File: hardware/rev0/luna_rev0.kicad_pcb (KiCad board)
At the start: 4 copper layers, 48.9 x 50 mm, 132 parts, among them IC1 ECP5-BGA256, J1 USB_B_Micro, J2 USB_B_Micro, J3 USB_A, J4 USB_B_Micro, J5 Conn_ARM_JTAG_SWD_10, J6 Conn_ARM_JTAG_SWD_10, J7 Conn_02x02_Counter_Clockwise, J8 Conn_Coaxial, J9 Conn_Coaxial, SW1 BTN_RECOVERY, SW2 BTN_DFU, SW3 BTN_RESET, U1 AP22814-SOT, U10 S27KS0641, U11 USB3343, U12 AP22814-SOT, U2 MIC5504-1.8YM5, U3 MIC5219-3.3YM5, U4 TCR2EE11, U5 MIC5504-2.5YM5, U6 ATSAMD21G18A-AUT, U7 W25Q32JVSS, U8 USB3343, U9 USB3343, Y1 DSC60xx

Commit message: hardware: rev0.2 (FFY00 + perigoso)
Signed-off-by: Filipe Laíns <lains@archlinux.org>
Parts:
- added G***: LOGO, ffy00-modules:brasao-smaller, B.Cu at (112.4, 90.2)
- J5, J6: footprint luna:SWD_CONNECTOR_LARGE_BOX -> Connector_PinHeader_2.00mm:PinHeader_2x05_P2.00mm_Vertical
- moved REF** 30.8 mm to (134.6, 73.7)
- moved J5 5.23 mm to (137.9, 100.8), turned to -90 degrees
- moved J6 2.98 mm to (129.9, 108.4), turned to 90 degrees
- moved G*** 1.74 mm to (97.8, 108.1)
- moved R25 1.65 mm to (140.1, 107.3)
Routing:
- net /FULL_RESET: track 34.6 -> 40.9 mm
- net /FPGA Configuration and Dev Features/FPGA_TMS: track 25.4 -> 28.1 mm
- net /FPGA Configuration and Dev Features/FPGA_TCK: track 23.7 -> 25.7 mm
- net /FPGA Configuration and Dev Features/FPGA_TDO: track 25.4 -> 26.7 mm
- net /FPGA Configuration and Dev Features/UC_SWDCLK: track 13.6 -> 14.8 mm
- net GND: track 180.0 -> 180.8 mm
- net /FPGA Configuration and Dev Features/FPGA_TDI: track 20.5 -> 21.1 mm
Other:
- net class Default removed
- board text added: "Filipe Laíns @FFY00 Rafael Silva @perigoso"
- board text added: "Manufactured by"
- board text removed: "3 G 0 2 G 1"
- board text removed: "A-Side"

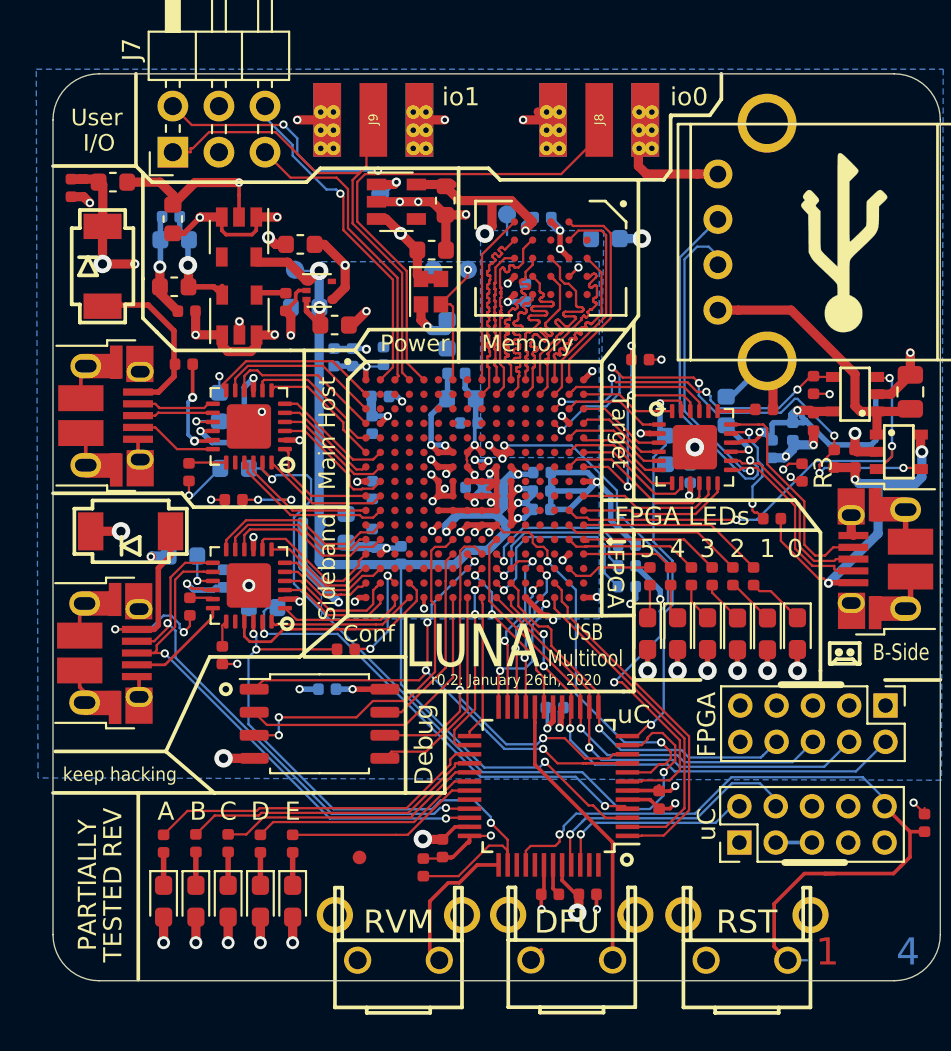
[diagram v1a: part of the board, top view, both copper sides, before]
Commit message: hardware: silkscreen fixups
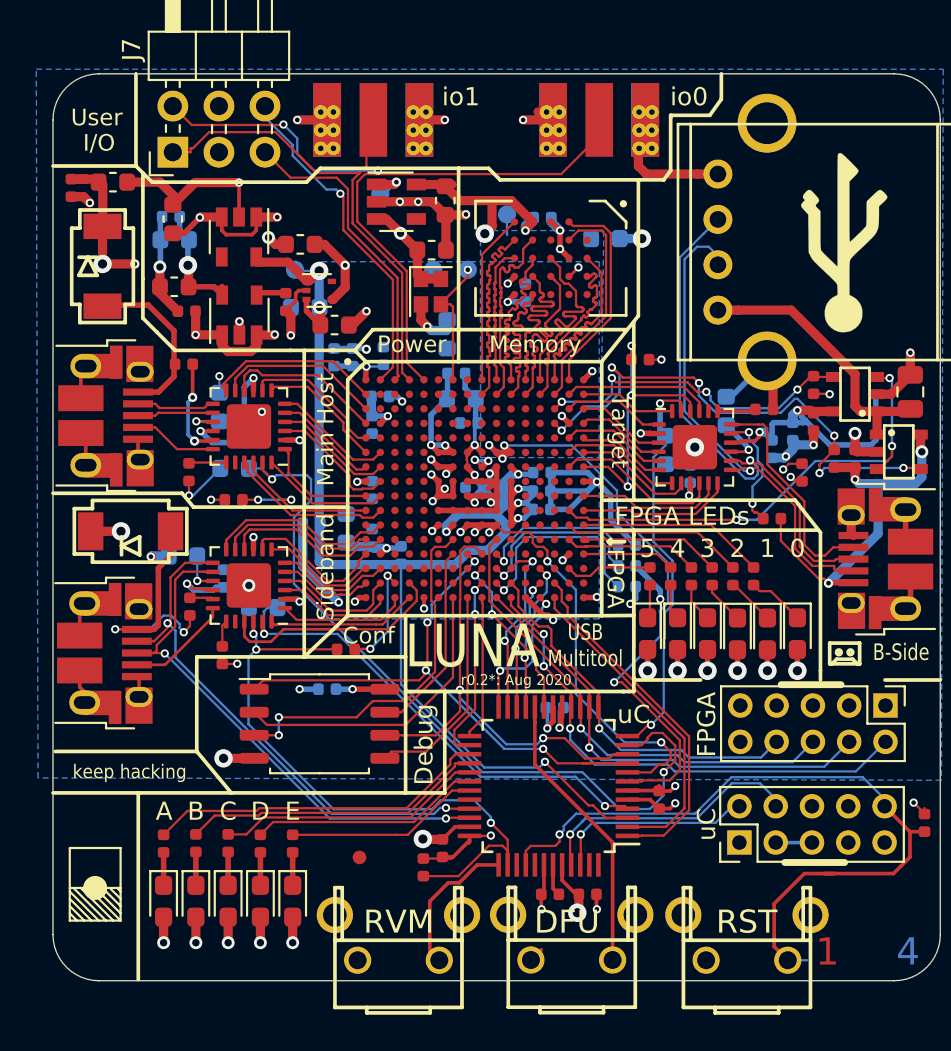
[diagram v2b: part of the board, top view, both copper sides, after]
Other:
- board text added: "Debug/Alt"
- board text added: "Port"
- board text added: "r0.2*: Aug 2020"
- board text removed: "Debug/Alt Port"
- board text removed: "PARTIALLY"
- board text removed: "TESTED REV"
- board text removed: "r0.2: January 26th, 2020"
